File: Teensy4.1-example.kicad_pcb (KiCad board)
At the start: 4 copper layers, 61.5 x 47.5 mm, 80 parts, among them IC1 MIMXRT1062DVJ6B, J1 Conn_01x11_Male, J2 Conn_01x11_Male, J3 Conn_01x12_Male, J4 Conn_01x11_Male, J5 Conn_01x11_Male, J6 Conn_01x03_Male, J7 Conn_01x03_Male, P2 D26, Q1 Q_PMOS_GDS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

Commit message: Migrate to kicad8
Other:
- board text removed: "Teensy 4.1 example board Feel free to use this as a starting point for your own boards, but pls do the fanout smarter (D41 got trapped and is not broken out). The board includes the required parts - MIMXRT1062DVJ6B (Arm Cortex M7 @ 600 Mhz) - MKL02Z32VFG4 (must be purchased from PJRC) - W25Q64JVXGIM (8Mb spi Flash) Optional parts (not in PJRC's design) - USB Type C for power & debug - USB Type C 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"

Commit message: Update layout
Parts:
- removed D2: LED, LED_SMD:LED_0402_1005Metric
- removed R6, R7: 16k, Resistor_SMD:R_0603_1608Metric
- removed R8: 1k, Resistor_SMD:R_0402_1005Metric
- removed U2: MAX1562, Package_SO:SO-8_3.9x4.9mm_P1.27mm
- added C27: 100uF, Capacitor_SMD:C_1206_3216Metric, F.Cu at (67.2, 104.2)
- added U5: TPD3S014DBVR, Package_TO_SOT_SMD:SOT-23-6, F.Cu at (70.5, 104.0)
- Q1: value Q_PMOS_GDS -> Q_PMOS_GDS_DMP3125L
- Y1: value Crystal_GND23 -> 24MHz
- Y2: value Crystal -> 32.768kHz
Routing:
- net +5VD: track 26.5 -> 18.6 mm, vias 5 -> 7
- net /USB2_DP: track 38.4 -> 45.2 mm
- net +5VL: track 20.2 -> 14.2 mm, vias 7 -> 9
- net Net-(R6-Pad2): track 5.05 -> 0.00 mm
- net Net-(IC1-GPIO_EMC_40): track 64.6 -> 69.4 mm
- net Net-(R7-Pad2): track 3.66 -> 0.00 mm
- net /USB2_DN: track 36.5 -> 39.4 mm
- net GND: track 47.4 -> 45.2 mm
- net Net-(D2-Pad1): track 1.51 -> 0.00 mm
- net /ONOFF: track 29.5 -> 30.1 mm
- added copper zone on F.Cu, net +5VD
- added copper zone on F.Cu, net +5VL

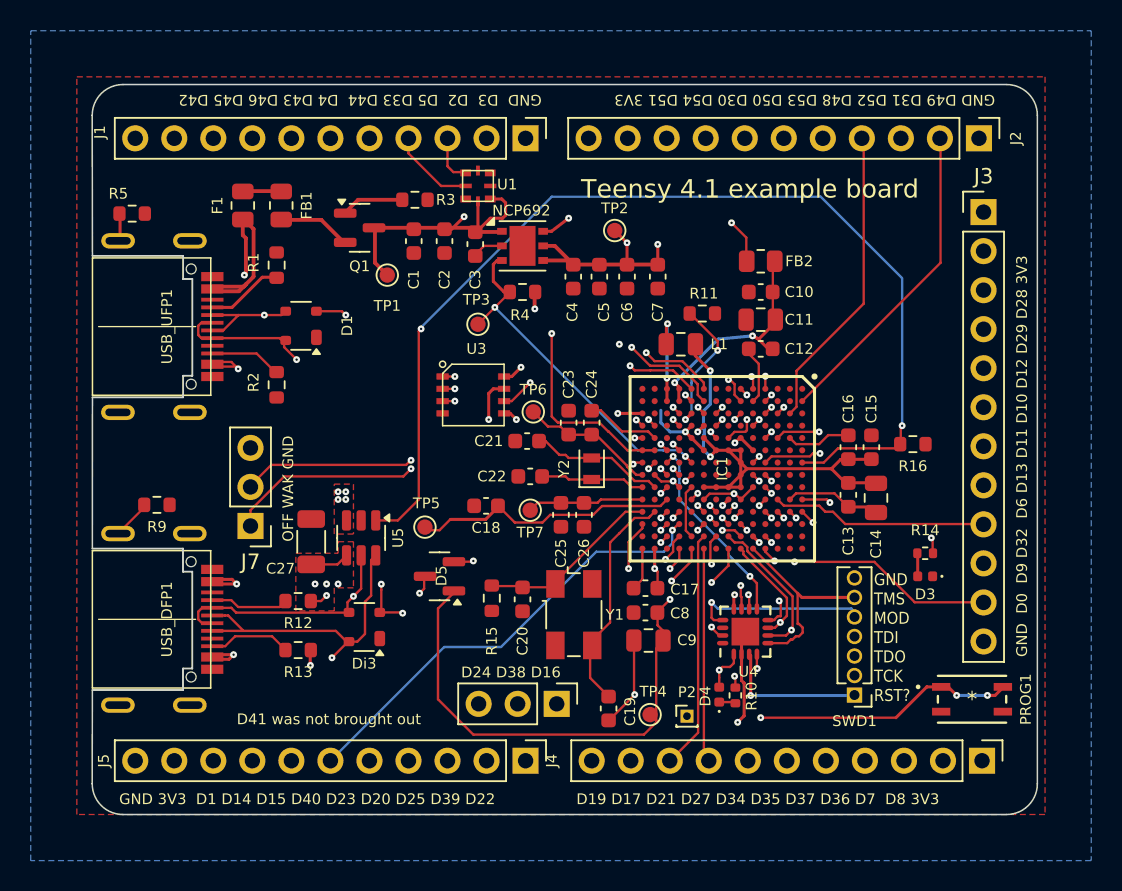
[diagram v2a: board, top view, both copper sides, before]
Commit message: Remove the RGB LED
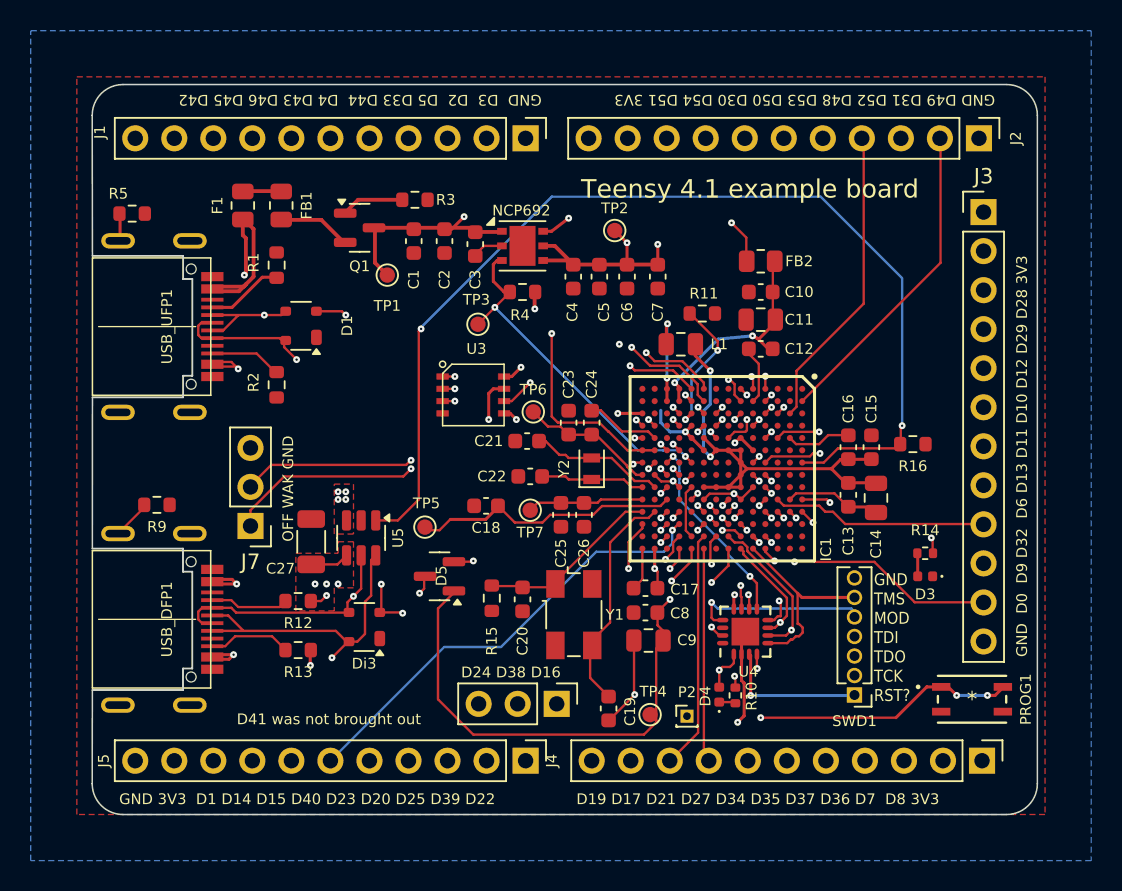
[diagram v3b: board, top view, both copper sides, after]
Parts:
- removed U1: opto_APA102-2020, USB-C-Power-tester:APA102-2020
- Q1: value Q_PMOS_GDS_DMP3125L -> DMP3125L
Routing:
- net +5V: track 34.4 -> 28.4 mm
- net /D5: track 34.1 -> 28.5 mm
- net /D2: track 30.1 -> 26.9 mm
